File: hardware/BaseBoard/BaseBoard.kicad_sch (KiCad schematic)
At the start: 89 parts, among them IC1 PCF8574RGTR, J1-ESP1 ESP-1-L, J1-ESP2 ESP-1-L, J1-ESP3 ESP-1-L, J1-ESP4 ESP-1-L, J1-ESP5 ESP-1-L, J1-ESP6 ESP-1-L, J1-ESP7 ESP-1-L, J1-ESP8 ESP-1-L, J2-ESP1 ESP-1-R, J2-ESP2 ESP-1-R, J2-ESP3 ESP-1-R, J2-ESP4 ESP-1-R, J2-ESP5 ESP-1-R, J2-ESP6 ESP-1-R, J2-ESP7 ESP-1-R, J2-ESP8 ESP-1-R, J3-BUS1 BUS-IN, J3-BUS2 BUS-IN, J3-BUS3 BUS-IN, J3-BUS4 BUS-IN, J3-BUS5 BUS-IN, J3-BUS6 BUS-IN, J3-BUS7 BUS-IN, J3-BUS8 BUS-IN, J4-BUS1 BUS-OUT, J4-BUS2 BUS-OUT, J4-BUS3 BUS-OUT, J4-BUS4 BUS-OUT, J4-BUS5 BUS-OUT, J4-BUS6 BUS-OUT, J4-BUS7 BUS-OUT, J4-BUS8 BUS-OUT, Q11 2N3904, Q12 AO3401A, Q21 2N3904, Q22 AO3401A, Q31 2N3904, Q32 AO3401A, Q41 2N3904, Q42 AO3401A, Q51 2N3904, Q52 AO3401A, Q61 2N3904, Q62 AO3401A, Q71 2N3904, Q72 AO3401A, Q81 2N3904, Q82 AO3401A, SW1 SW_DIP_SPSTx03, U1 AMS1117-3.3

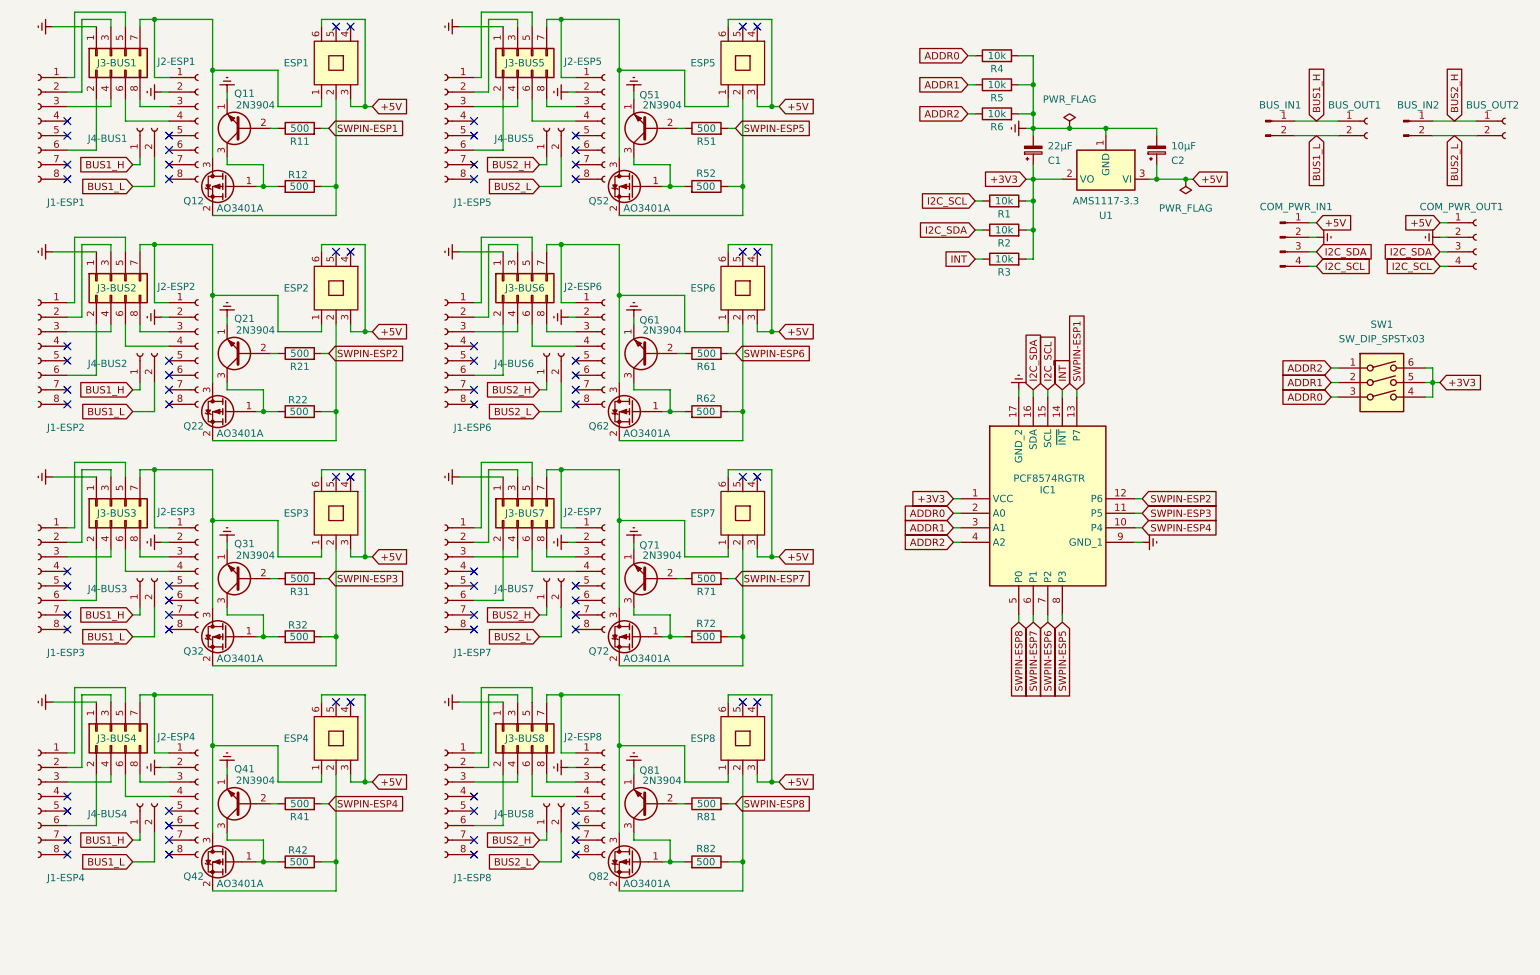
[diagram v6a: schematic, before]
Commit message: Simplified BaseBoard.
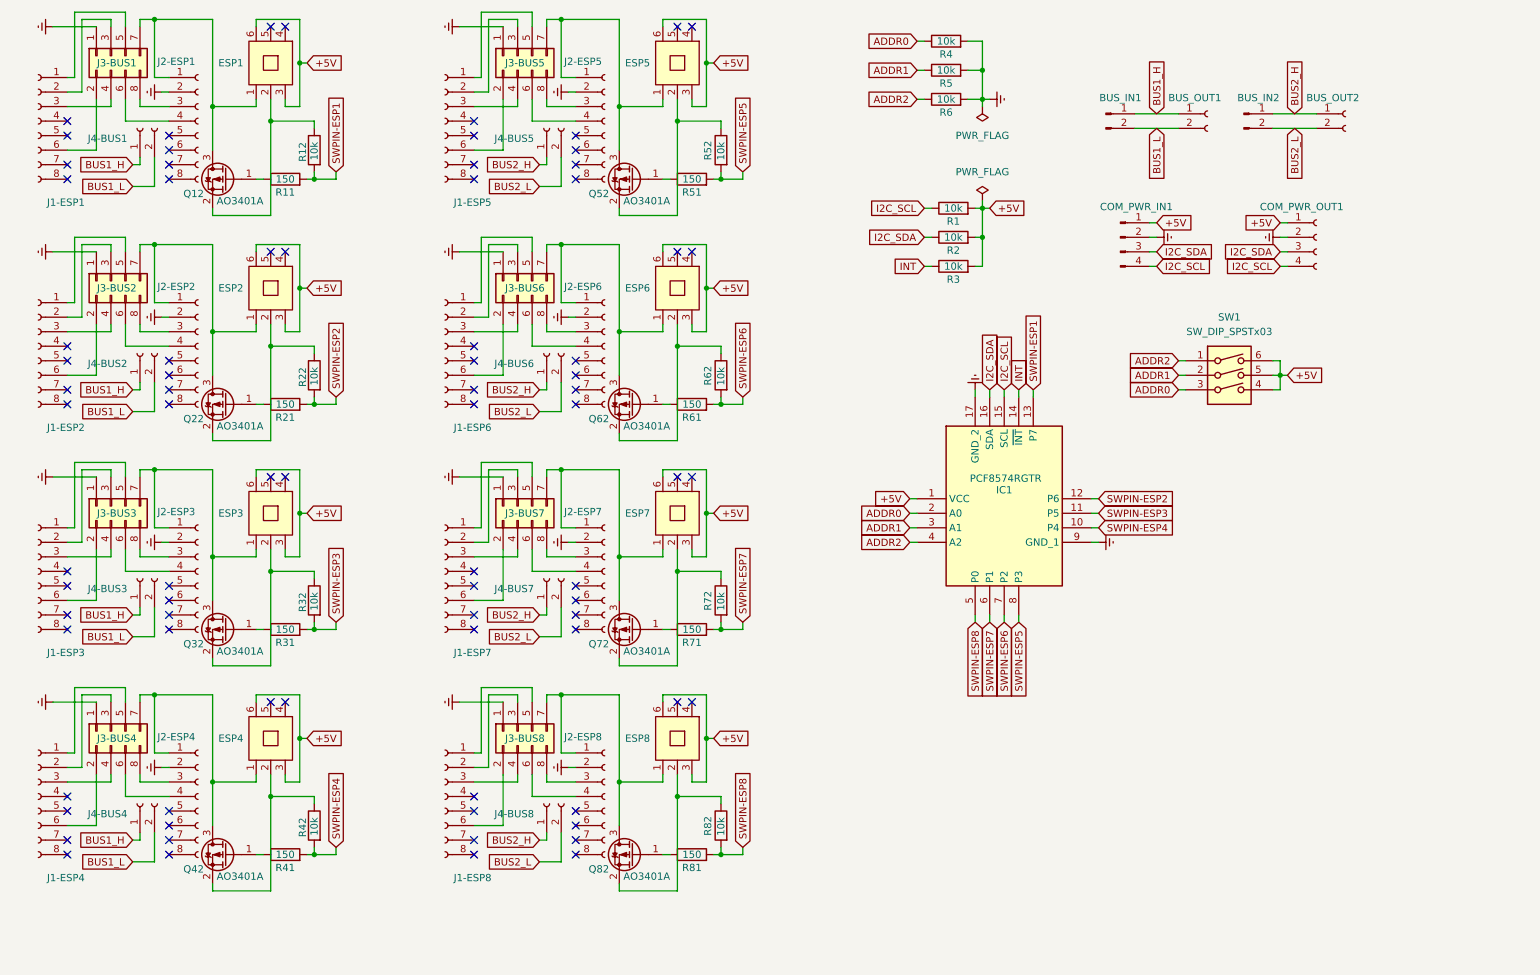
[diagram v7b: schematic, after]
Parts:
- removed C1: 22µF, Capacitor_SMD:CP_Elec_4x5.3, symbol Device:C_Polarized_Small
- removed C2: 10µF, Capacitor_SMD:CP_Elec_4x5.3, symbol Device:C_Polarized_Small
- removed Q11, Q21, Q31, Q41, Q51, Q61, Q71, Q81: 2N3904, Package_TO_SOT_THT:TO-92_Inline, symbol Transistor_BJT:2N3904
- removed U1: AMS1117-3.3, Package_TO_SOT_SMD:SOT-223-3_TabPin2, symbol Regulator_Linear:AMS1117-3.3
- R11, R21, R31, R41, R51, R61, R71, R81: value 500 -> 150; footprint Resistor_SMD:R_0603_1608Metric -> Resistor_SMD:R_0402_1005Metric
- R12, R22, R32, R42, R52, R62, R72, R82: value 500 -> 10k; footprint Resistor_SMD:R_0603_1608Metric -> Resistor_SMD:R_0402_1005Metric
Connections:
- net +3V3 is gone; now on net +5V: IC1.1 (VCC), R1.2, R2.2, R3.2, SW1.4, SW1.5, SW1.6
- net SWPIN-ESP1: now also R12.2
- net SWPIN-ESP2: now also R22.2
- net SWPIN-ESP3: now also R32.2
- net SWPIN-ESP4: now also R42.2
- net SWPIN-ESP5: now also R52.2
- net SWPIN-ESP6: now also R62.2
- net SWPIN-ESP7: now also R72.2
- net SWPIN-ESP8: now also R82.2
- net at Q22.1 (G): now also R21.1; no longer R22.2
- net at R51.1: now also Q52.1 (G)
- net at R61.1: now also Q62.1 (G)
- net at R71.1: now also Q72.1 (G)
- net at R11.1: now also Q12.1 (G)
- net at Q42.1 (G): now also R41.1; no longer R42.2
- net at Q32.1 (G): now also R31.1; no longer R32.2
- net at R81.1: now also Q82.1 (G)
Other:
- moved on the sheet: BUS_IN1, BUS_IN2, BUS_OUT1, BUS_OUT2, COM_PWR_IN1, COM_PWR_OUT1, ESP1, ESP2, ESP3, ESP4, ESP5, ESP6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

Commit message: Minor BaseBoard updates.
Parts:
- added R7: 50, Resistor_SMD:R_0603_1608Metric, symbol Device:R
- renumbered Q12 to Q1, Q22 to Q2, Q32 to Q3, Q42 to Q4, Q52 to Q5, Q62 to Q6, Q72 to Q7, Q82 to Q8
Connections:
- net +5V: now also R7.2; no longer IC1.1 (VCC), R1.2, R2.2, R3.2, SW1.4, SW1.5, SW1.6
- new net +5VSwitching: IC1.1 (VCC), R1.2, R2.2, R3.2, R7.1, SW1.4, SW1.5, SW1.6
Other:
- moved on the sheet: R1, R2, R3, R4, R5, R6
